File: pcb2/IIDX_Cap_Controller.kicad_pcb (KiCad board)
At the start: 2 copper layers, 198.6 x 99.1 mm, 12 parts, among them J11 Conn_01x07_Pin, J4 Conn_01x01, J8 Conn_01x07_Pin, J9 Conn_01x07_Pin

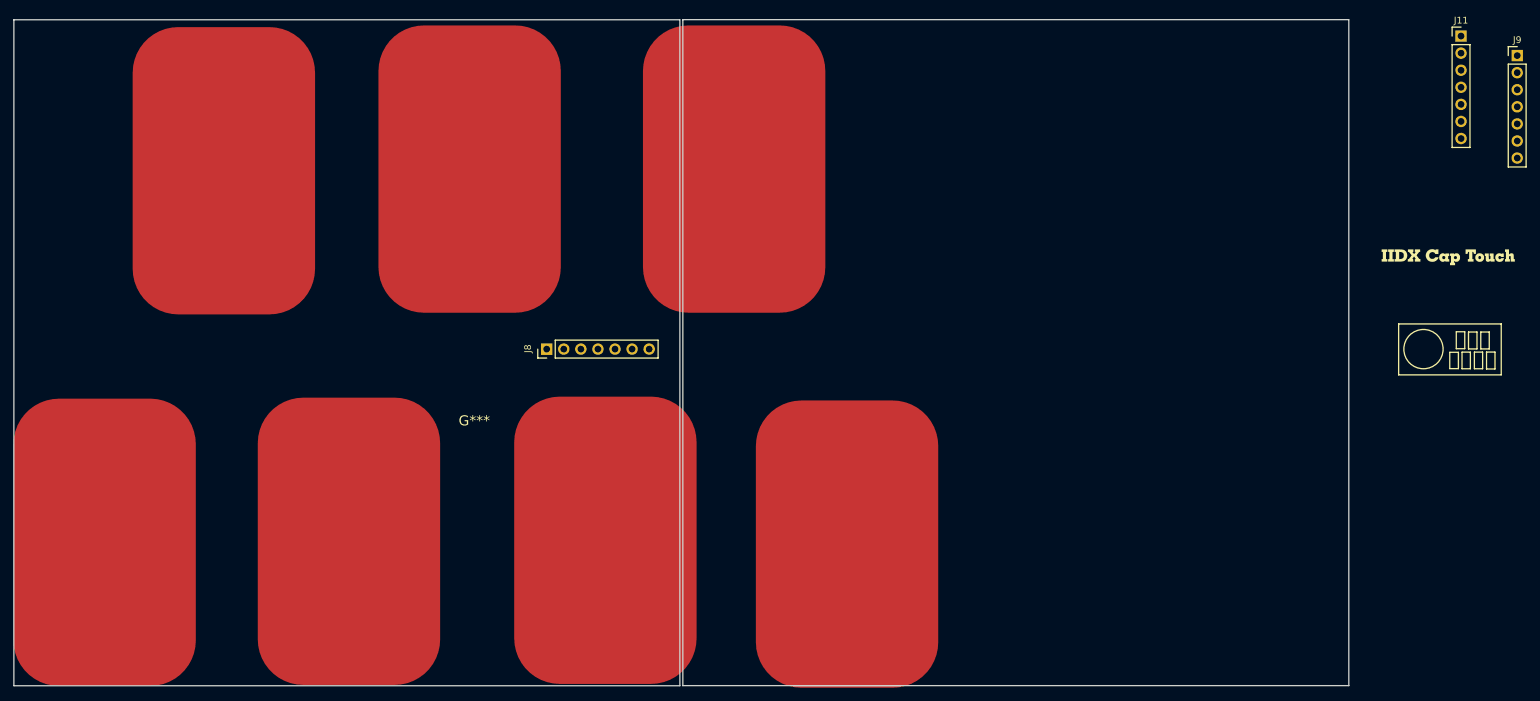
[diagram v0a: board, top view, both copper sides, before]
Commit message: feat: layout & routing with pico onboard
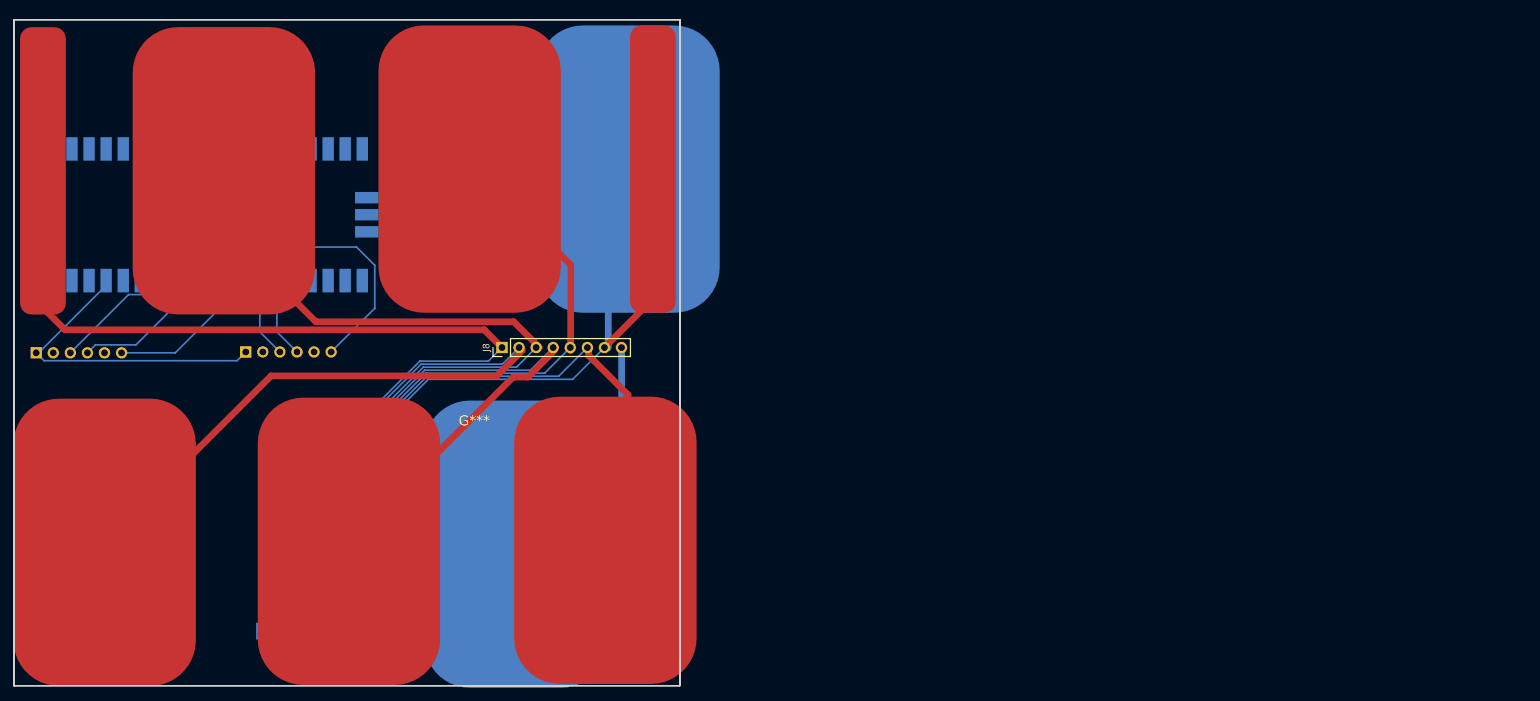
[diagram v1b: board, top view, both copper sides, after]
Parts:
- added G***: LOGO, LOGO, B.Cu at (89.9, 35.3)
- added J10: Conn_01x06, Connector_PinHeader_2.54mm:PinHeader_1x06_P2.54mm_Vertical, B.Cu at (100.6, 81.3)
- added J12: Conn_01x05_Pin, Connector_PinHeader_2.54mm:PinHeader_1x08_P2.54mm_Vertical_SMD_Pin1Left, B.Cu at (142.7, 124.4)
- added J6: Conn_01x01, clipboard:4807e8d7-bff8-4c85-8422-397af0b06065, F.Cu at (188.1, 32.2)
- added RP0: Conn_02x20_Counter_Clockwise, RPi_Pico_SMD_TH, B.Cu at (125.0, 60.8)
- G***: moved to B.Cu
- J11: value Conn_01x07_Pin -> Conn_01x06; footprint Connector_PinHeader_2.54mm:PinHeader_1x07_P2.54mm_Vertical -> Connector_PinHeader_2.54mm:PinHeader_1x06_P2.54mm_Vertical; moved to B.Cu
- J6, J7: renamed from J4; moved to B.Cu
- J8: value Conn_01x07_Pin -> Conn_01x05_Pin; footprint Connector_PinHeader_2.54mm:PinHeader_1x07_P2.54mm_Vertical -> Connector_PinHeader_2.54mm:PinHeader_1x08_P2.54mm_Vertical
- J9: value Conn_01x07_Pin -> Conn_01x01; footprint Connector_PinHeader_2.54mm:PinHeader_1x07_P2.54mm_Vertical -> clipboard:4807e8d7-bff8-4c85-8422-397af0b06065
- moved J9 223.6 mm to (97.4, 32.4)
- moved J11 186.8 mm to (131.8, 81.2), turned to -90 degrees
- moved G*** 162.8 mm to (171.2, 32.5), turned to 90 degrees
- moved J7 20.5 mm to (186.3, 88.0), turned to 180 degrees
- moved J6 13.0 mm to (203.1, 32.2), turned to 180 degrees
- moved J8 6.66 mm to (169.9, 80.5)
- renumbered J4 to J1, J4 to J2, J4 to J3, J4 to J5
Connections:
- J1 pad 1: (no net) -> Net-(J1-Pin_1)
- J11 pad 1: unconnected-(J11-Pin_1-Pad1) -> +3.3V
- J11 pad 3: unconnected-(J11-Pin_3-Pad3) -> /SCL2
- J11 pad 4: unconnected-(J11-Pin_4-Pad4) -> /SDA2
- J11 pad 6: unconnected-(J11-Pin_6-Pad6) -> GND
- J2 pad 1: Net-(J4-Pin_1) -> Net-(J12-Pin_3)
- J3 pad 1: (no net) -> Net-(J12-Pin_4)
- J4 pad 1: (no net) -> Net-(J12-Pin_5)
- J5 pad 1: (no net) -> Net-(J12-Pin_6)
- J6 pad 1: (no net) -> Net-(J12-Pin_7)
- J7 pad 1: (no net) -> Net-(J12-Pin_8)
- J8 pad 1: Net-(J1-Pin_1) -> Net-(J12-Pin_1)
- J8 pad 2: Net-(J2-Pin_1) -> Net-(J1-Pin_1)
- J8 pad 3: Net-(J3-Pin_1) -> Net-(J12-Pin_3)
- J8 pad 4: Net-(J4-Pin_1) -> Net-(J12-Pin_4)
- J8 pad 5: Net-(J5-Pin_1) -> Net-(J12-Pin_5)
- J8 pad 6: Net-(J6-Pin_1) -> Net-(J12-Pin_6)
- J8 pad 7: Net-(J7-Pin_1) -> Net-(J12-Pin_7)
- J9 pad 1: unconnected-(J9-Pin_1-Pad1) -> Net-(J12-Pin_1)
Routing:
- net Net-(J12-Pin_1): track 0.00 -> 154.2 mm
- net Net-(J1-Pin_1): track 0.00 -> 141.5 mm
- net Net-(J12-Pin_3): track 0.00 -> 128.2 mm
- net Net-(J12-Pin_7): track 0.00 -> 126.6 mm
- net Net-(J12-Pin_4): track 0.00 -> 112.1 mm
- net Net-(J12-Pin_6): track 0.00 -> 103.9 mm
- net Net-(J12-Pin_5): track 0.00 -> 101.2 mm
- net Net-(J12-Pin_8): track 0.00 -> 62.8 mm
- net GND: track 0.00 -> 61.8 mm
- net +3.3V: track 0.00 -> 48.4 mm
- net /SDA1: track 0.00 -> 21.6 mm
- net /SCL1: track 0.00 -> 21.3 mm
- net /SDA2: track 0.00 -> 12.8 mm
- net /SCL2: track 0.00 -> 12.8 mm
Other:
- board size 198.6 x 99.1 mm -> 99.1 x 99.1 mm
- board text added: "RPi Pico Captouch Board"

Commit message: feat: production 2
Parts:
- moved G*** 4.56 mm to (170.9, 28.0)
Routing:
- net GND: track 61.8 -> 89.3 mm
- net Net-(J12-Pin_5): track 101.2 -> 100.2 mm
- net Net-(J12-Pin_6): track 103.9 -> 104.7 mm
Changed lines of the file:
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@@
   )
   (footprint "LOGO" (layer "B.Cu")
-    (at 171.200729 32.506183 90)
+    (at 170.870488 27.962665 90)
     (attr board_only exclude_from_pos_files exclude_from_bom)
     (fp_text reference "G***" (at -20.184397 3.339864 90) (layer "B.SilkS") hide
@@
     )
   )
-  (gr_rect (start 163.195663 50.287892) (end 165.712992 51.547655)
+  (gr_rect (start 162.768051 44.955199) (end 165.28538 46.214962)
     (stroke (width 0.15) (type default)) (fill none) (layer "B.SilkS"))
-  (gr_rect (start 127.301449 37.571005) (end 128.561212 35.053676)
+  (gr_rect (start 127.301449 35.053676) (end 128.561212 37.571005)
     (stroke (width 0.15) (type default)) (fill none) (layer "B.SilkS"))
-  (gr_rect (start 121.875496 41.464733) (end 137.137118 33.885833)
+  (gr_rect (start 121.875496 33.885833) (end 137.137118 41.464733)
     (stroke (width 0.15) (type default)) (fill none) (layer "B.SilkS"))
-  (gr_rect (start 159.301935 44.861939) (end 166.880835 60.123561)
+  (gr_rect (start 158.874323 39.529246) (end 166.453223 54.790868)
     (stroke (width 0.15) (type default)) (fill none) (layer "B.SilkS"))
   (gr_rect (start 123.206259 78.74) (end 153.507784 118.888093)
     (stroke (width 0.2) (type default)) (fill none) (layer "B.SilkS"))
-  (gr_circle (center 163.133408 56.430516) (end 160.898794 54.551858)
+  (gr_circle (center 162.705796 51.097823) (end 160.471182 49.219165)
     (stroke (width 0.15) (type default)) (fill none) (layer "B.SilkS"))
-  (gr_rect (start 122.804388 40.588576) (end 124.064151 38.071247)
+  (gr_rect (start 122.804388 38.071247) (end 124.064151 40.588576)
     (stroke (width 0.15) (type default)) (fill none) (layer "B.SilkS"))
-  (gr_rect (start 160.211601 47.630671) (end 162.689561 48.856559)
+  (gr_rect (start 159.783989 42.297978) (end 162.261949 43.523866)
     (stroke (width 0.15) (type default)) (fill none) (layer "B.SilkS"))
-  (gr_rect (start 125.485047 37.606161) (end 126.74481 35.088832)
+  (gr_rect (start 125.485047 35.088832) (end 126.74481 37.606161)
     (stroke (width 0.15) (type default)) (fill none) (layer "B.SilkS"))
   (gr_line (start 154.832506 31.418221) (end 154.950635 130.471881)
@@
   (gr_circle (center 133.444073 37.63326) (end 131.565415 39.867874)
     (stroke (width 0.15) (type default)) (fill none) (layer "B.SilkS"))
-  (gr_rect (start 160.230827 51.234178) (end 162.660265 52.517378)
+  (gr_rect (start 159.803215 45.901485) (end 162.232653 47.184685)
     (stroke (width 0.15) (type default)) (fill none) (layer "B.SilkS"))
   (gr_rect (start 92.020682 78.736795) (end 122.322207 118.884888)
     (stroke (width 0.2) (type default)) (fill none) (layer "B.SilkS"))
-  (gr_rect (start 160.178092 45.790831) (end 162.695421 47.050594)
+  (gr_rect (start 159.75048 40.458138) (end 162.267809 41.717901)
     (stroke (width 0.15) (type default)) (fill none) (layer "B.SilkS"))
-  (gr_rect (start 123.656926 37.606161) (end 124.916689 35.088832)
+  (gr_rect (start 123.656926 35.088832) (end 124.916689 37.606161)
     (stroke (width 0.15) (type default)) (fill none) (layer "B.SilkS"))
-  (gr_rect (start 124.644228 40.555067) (end 125.870116 38.077107)
+  (gr_rect (start 124.644228 38.077107) (end 125.870116 40.555067)
     (stroke (width 0.15) (type default)) (fill none) (layer "B.SilkS"))
-  (gr_rect (start 126.466489 40.555067) (end 127.709223 38.082966)
+  (gr_rect (start 126.466489 38.082966) (end 127.709223 40.555067)
     (stroke (width 0.15) (type default)) (fill none) (layer "B.SilkS"))
-  (gr_rect (start 163.160507 46.643369) (end 165.677836 47.903132)
+  (gr_rect (start 162.732895 41.310676) (end 165.250224 42.570439)
     (stroke (width 0.15) (type default)) (fill none) (layer "B.SilkS"))
-  (gr_rect (start 160.211601 49.452932) (end 162.683702 50.695666)
+  (gr_rect (start 159.783989 44.120239) (end 162.25609 45.362973)
     (stroke (width 0.15) (type default)) (fill none) (layer "B.SilkS"))
-  (gr_rect (start 163.160507 48.47149) (end 165.677836 49.731253)
+  (gr_rect (start 162.732895 43.138797) (end 165.250224 44.39856)
     (stroke (width 0.15) (type default)) (fill none) (layer "B.SilkS"))
-  (gr_rect (start 128.247735 40.535841) (end 129.530935 38.106403)
+  (gr_rect (start 128.247735 38.106403) (end 129.530935 40.535841)
     (stroke (width 0.15) (type default)) (fill none) (layer "B.SilkS"))
-  (gr_rect (start 97.299566 130.8247) (end 196.359566 31.7647)
-    (stroke (width 0.1) (type default)) (fill none) (layer "Edge.Cuts"))
   (gr_rect (start 97.300026 31.772913) (end 196.360026 130.832913)
     (stroke (width 0.1) (type default)) (fill none) (layer "Edge.Cuts"))
@@
   (segment (start 150.981441 74.68734) (end 150.981441 68.288858) (width 0.25) (layer "B.Cu") (net 37))
   (segment (start 113.319644 81.310065) (end 121.309682 81.310065) (width 0.25) (layer "B.Cu") (net 37))
+  (segment (start 108.399757 67.20999) (end 128.889551 67.20999) (width 0.25) (layer "B.Cu") (net 37))
   (segment (start 135.427016 65.582731) (end 131.344654 69.665093) (width 0.25) (layer "B.Cu") (net 37))
   (segment (start 144.488508 81.180273) (end 150.981441 74.68734) (width 0.25) (layer "B.Cu") (net 37))
   (segment (start 131.344654 71.275093) (end 131.344654 69.665093) (width 0.25) (layer "B.Cu") (net 37))
   (segment (start 150.981441 68.288858) (end 148.275314 65.582731) (width 0.25) (layer "B.Cu") (net 37))
+  (segment (start 105.944654 69.665093) (end 108.399757 67.20999) (width 0.25) (layer "B.Cu") (net 37))
+  (segment (start 128.889551 67.20999) (end 131.344654 69.665093) (width 0.25) (layer "B.Cu") (net 37))
   (segment (start 105.699644 81.310065) (end 114.369616 72.640093) (width 0.25) (layer "B.Cu") (net 38))
   (segment (start 121.184654 71.275093) (end 121.184654 69.665093) (width 0.25) (layer "B.Cu") (net 38))
@@
   (segment (start 138.907731 102.744647) (end 138.907731 122.713728) (width 0.25) (layer "B.Cu") (net 45))
   (segment (start 172.061003 83.446158) (end 158.20622 83.446158) (width 0.25) (layer "B.Cu") (net 45))
-  (segment (start 147.142409 109.346366) (end 171.565256 84.923519) (width 1) (layer "F.Cu") (net 46))
-  (segment (start 173.751593 84.923519) (end 177.782407 80.892705) (width 1) (layer "F.Cu") (net 46))
-  (segment (start 171.565256 84.923519) (end 173.751593 84.923519) (width 1) (layer "F.Cu") (net 46))
+  (segment (start 147.142409 109.346366) (end 149.328746 109.346366) (width 1) (layer "F.Cu") (net 46))
+  (segment (start 149.328746 109.346366) (end 177.782407 80.892705) (width 1) (layer "F.Cu") (net 46))
   (segment (start 177.519833 80.527328) (end 174.151003 83.896158) (width 0.25) (layer "B.Cu") (net 46))
   (segment (start 174.151003 83.896158) (end 158.392616 83.896158) (width 0.25) (layer "B.Cu") (net 46))
   (segment (start 141.447731 100.841043) (end 141.447731 126.023728) (width 0.25) (layer "B.Cu") (net 46))
   (segment (start 158.392616 83.896158) (end 141.447731 100.841043) (width 0.25) (layer "B.Cu") (net 46))
-  (segment (start 165.842663 53.980909) (end 180.121651 68.259897) (width 1) (layer "F.Cu") (net 47))
-  (segment (start 165.091829 53.980909) (end 165.842663 53.980909) (width 1) (layer "F.Cu") (net 47))
-  (segment (start 180.121651 68.259897) (end 180.121651 81.019151) (width 1) (layer "F.Cu") (net 47))
+  (segment (start 165.091829 65.559324) (end 180.059833 80.527328) (width 1) (layer "F.Cu") (net 47))
+  (segment (start 165.091829 53.980909) (end 165.091829 65.559324) (width 1) (layer "F.Cu") (net 47))
   (segment (start 176.241003 84.346158) (end 158.579012 84.346158) (width 0.25) (layer "B.Cu") (net 47))
   (segment (start 158.579012 84.346158) (end 143.987731 98.937439) (width 0.25) (layer "B.Cu") (net 47))
   (segment (start 180.059833 80.527328) (end 176.241003 84.346158) (width 0.25) (layer "B.Cu") (net 47))
   (segment (start 143.987731 98.937439) (end 143.987731 122.713728) (width 0.25) (layer "B.Cu") (net 47))
-  (segment (start 185.285341 92.150345) (end 188.646932 88.788754) (width 1) (layer "F.Cu") (net 48))
-  (segment (start 188.646932 87.552913) (end 182.808621 81.714602) (width 1) (layer "F.Cu") (net 48))
-  (segment (start 182.808621 81.714602) (end 182.808621 81.050762) (width 1) (layer "F.Cu") (net 48))
-  (segment (start 188.646932 88.788754) (end 188.646932 87.552913) (width 1) (layer "F.Cu") (net 48))
+  (segment (start 185.285341 92.150345) (end 189.608124 87.827562) (width 1) (layer "F.Cu") (net 48))
   (segment (start 185.285341 109.196197) (end 185.285341 92.150345) (width 1) (layer "F.Cu") (net 48))
+  (segment (start 189.608124 87.827562) (end 182.808621 81.028059) (width 1) (layer "F.Cu") (net 48))
+  (segment (start 182.808621 81.028059) (end 182.808621 81.050762) (width 1) (layer "F.Cu") (net 48))
   (segment (start 158.765408 84.796158) (end 146.527731 97.033835) (width 0.25) (layer "B.Cu") (net 48))
   (segment (start 178.331003 84.796158) (end 158.765408 84.796158) (width 0.25) (layer "B.Cu") (net 48))
